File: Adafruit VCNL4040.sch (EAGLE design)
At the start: 14 parts, among them Q2 BSS138, U1 VCNL4040M3OE, U2 AP2112K-3.3

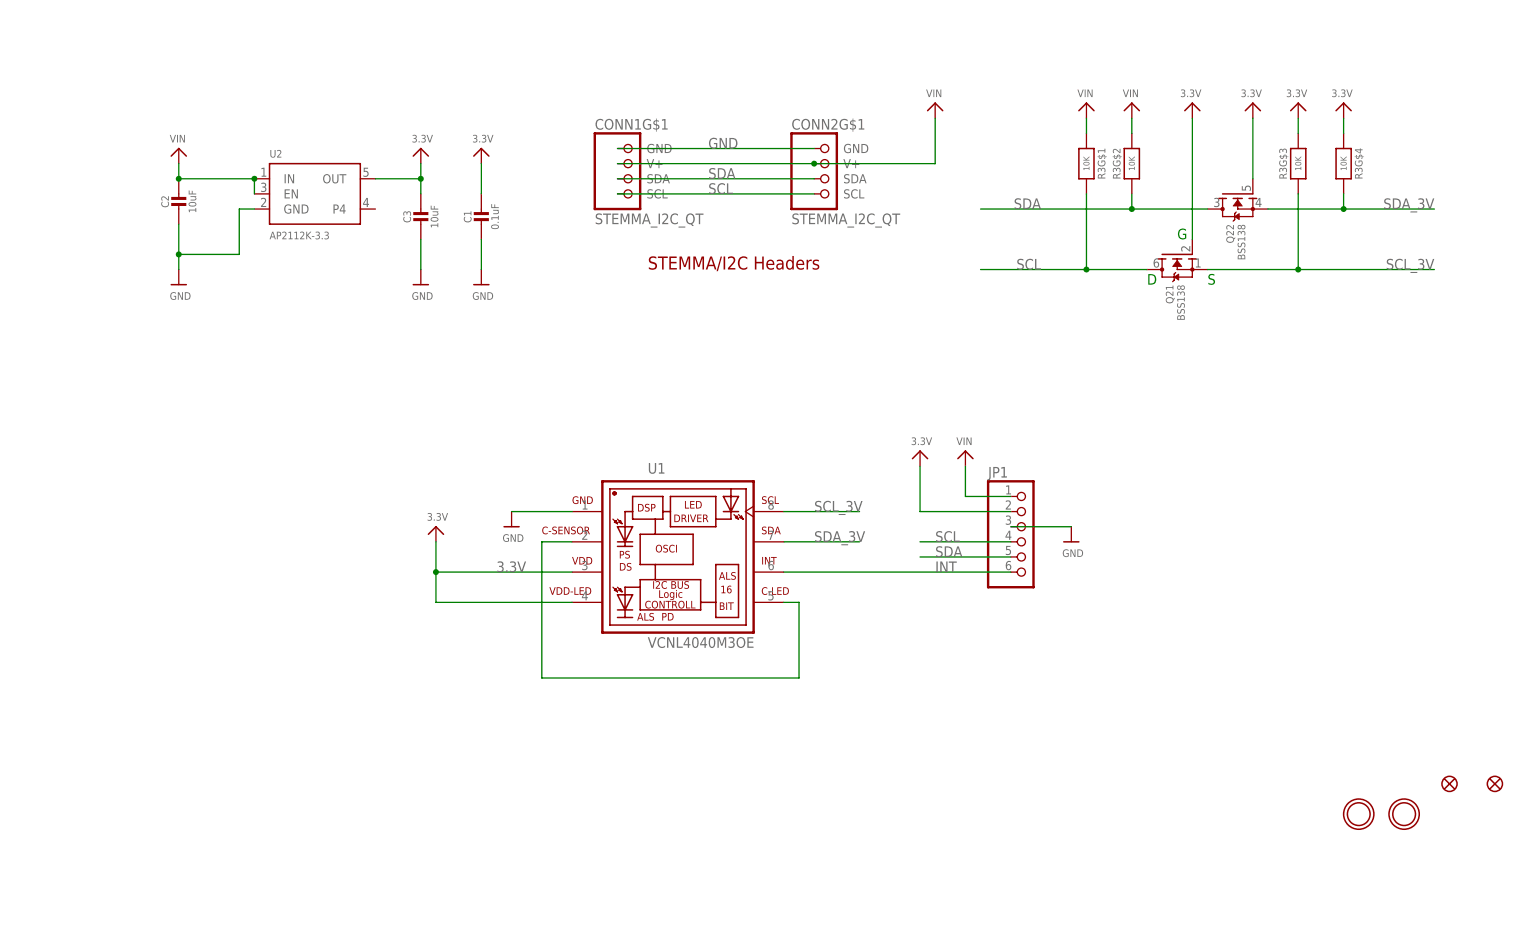
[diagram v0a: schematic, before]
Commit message: setup with cookiecutter and latest pcb rev.
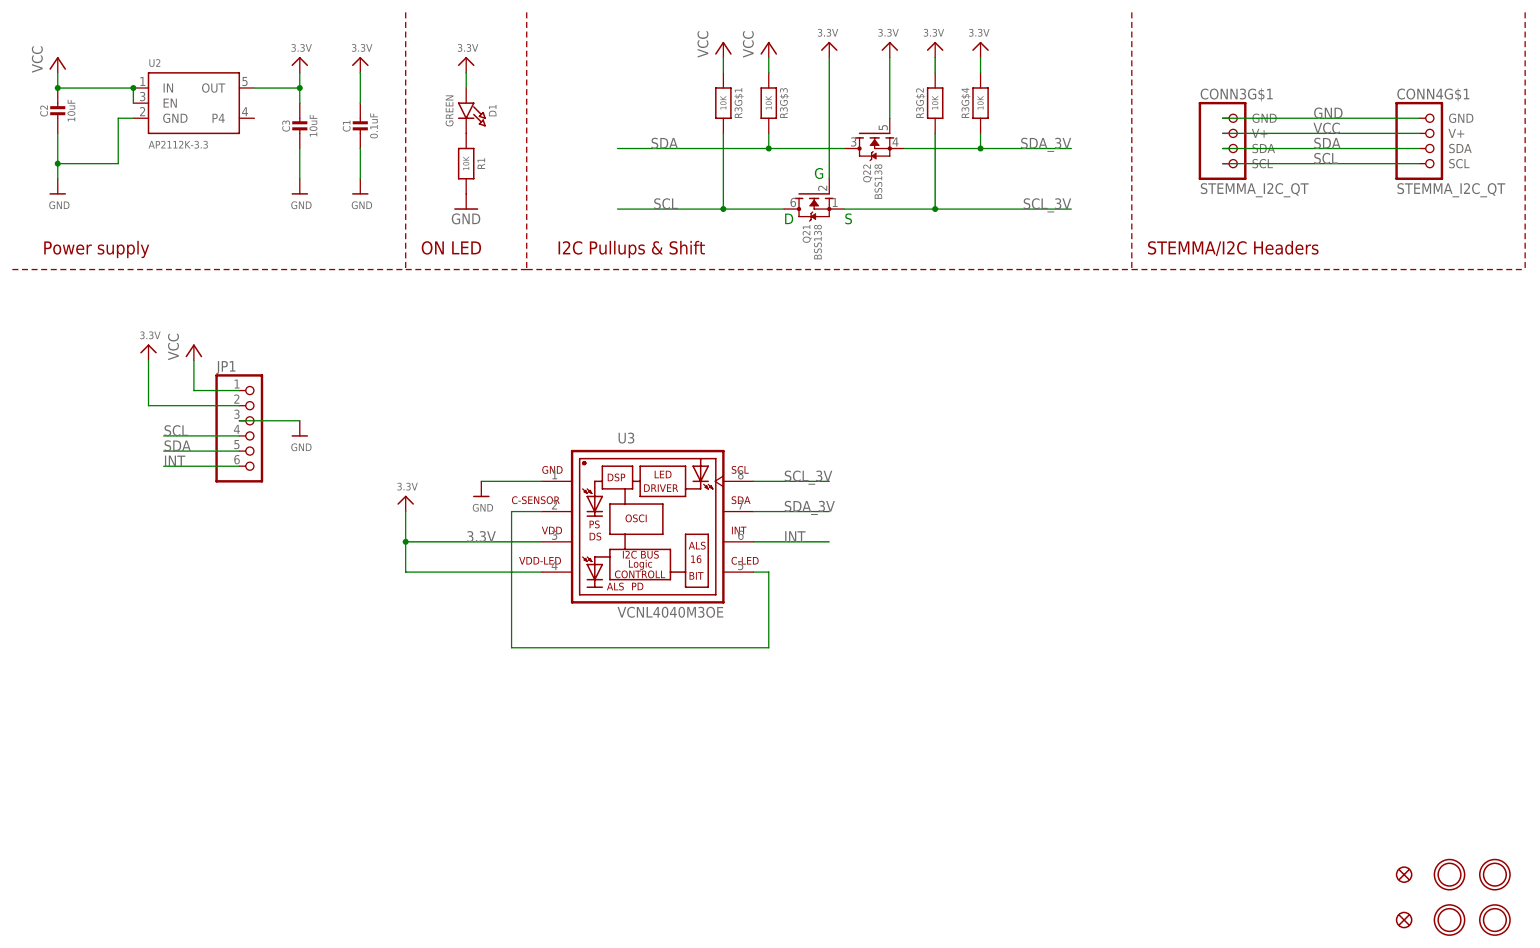
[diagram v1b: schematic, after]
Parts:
- removed CONN1, CONN2: STEMMA_I2C_QT, microbuilder:STEMMA_I2C_QT
- removed FID1, FID2: FIDUCIAL_1MM, microbuilder:FIDUCIAL_1MM
- removed U$3, U$4: MOUNTINGHOLE2.5, microbuilder:MOUNTINGHOLE2.5
- removed U1: VCNL4040M3OE, VCNL4040M3OE:VCNL4040M3OE
- added CONN3, CONN4: STEMMA_I2C_QT, microbuilder:STEMMA_I2C_QT
- added D1: GREEN, microbuilder:LED0603_NOOUTLINE
- added FID3, FID4: FIDUCIAL_1MM, microbuilder:FIDUCIAL_1MM
- added R1: 10K, microbuilder:RESISTOR_0603_NOOUT
- added U$1, U$17, U$19, U$21: MOUNTINGHOLE2.5, microbuilder:MOUNTINGHOLE2.5
- added U3: VCNL4040M3OE, VCNL4040M3OE:VCNL4040M3OE
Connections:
- removed net VIN: C2.1, CONN1G$1.V+, CONN2G$1.V+, JP1.1, R3G$1.1, R3G$2.1, U2.EN, U2.IN
- new net N$2: D1.C, R1.1
- new net VCC: C2.1, CONN3G$1.V+, CONN4G$1.V+, JP1.1, R3G$1.1, R3G$3.1, U2.EN, U2.IN
- net 3.3V: now also D1.A, R3G$2.1, R3G$4.1, U3.VDD, U3.VDD-LED; no longer R3G$3.2, R3G$4.2, U1.VDD, U1.VDD-LED
- net CATHODE: now also U3.C-LED, U3.C-SENSOR; no longer U1.C-LED, U1.C-SENSOR
- net GND: now also CONN3G$1.GND, CONN4G$1.GND, R1.2, U3.GND; no longer CONN1G$1.GND, CONN2G$1.GND, U1.GND
- net INT: now also U3.INT; no longer U1.INT
- net SCL: now also CONN3G$1.SCL, CONN4G$1.SCL; no longer CONN1G$1.SCL, CONN2G$1.SCL
- net SCL_3V: now also R3G$2.2, U3.SCL; no longer R3G$3.1, U1.SCL
- net SDA: now also CONN3G$1.SDA, CONN4G$1.SDA, R3G$3.2; no longer CONN1G$1.SDA, CONN2G$1.SDA, R3G$2.2
- net SDA_3V: now also R3G$4.2, U3.SDA; no longer R3G$4.1, U1.SDA
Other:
- note added: "I2C Pullups & Shift"
- note added: "ON LED"
- note added: "Power supply"
- moved on the sheet: C1, C2, C3, JP1, Q21, Q22, R3G$1, R3G$2, R3G$3, R3G$4, U2
